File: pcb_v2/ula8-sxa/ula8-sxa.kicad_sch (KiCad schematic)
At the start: 7 parts, among them J1 ula8a, U1 74LS244

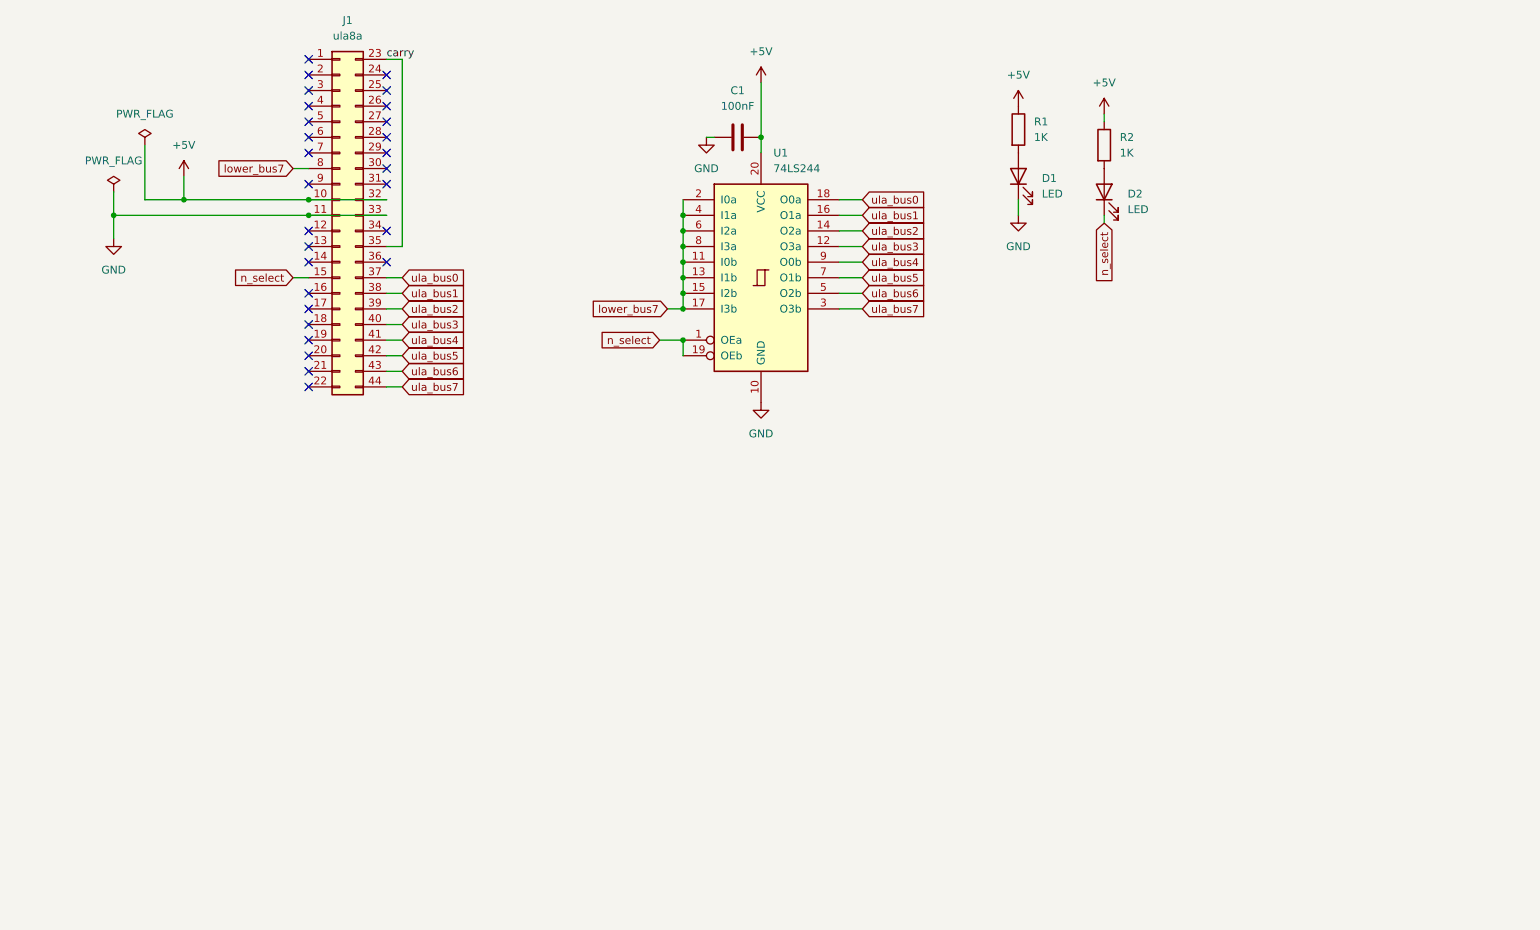
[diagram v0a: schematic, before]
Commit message: deslocando alimentação para as estremidades do conector; carry out em três estados (ativo apenas quando select)
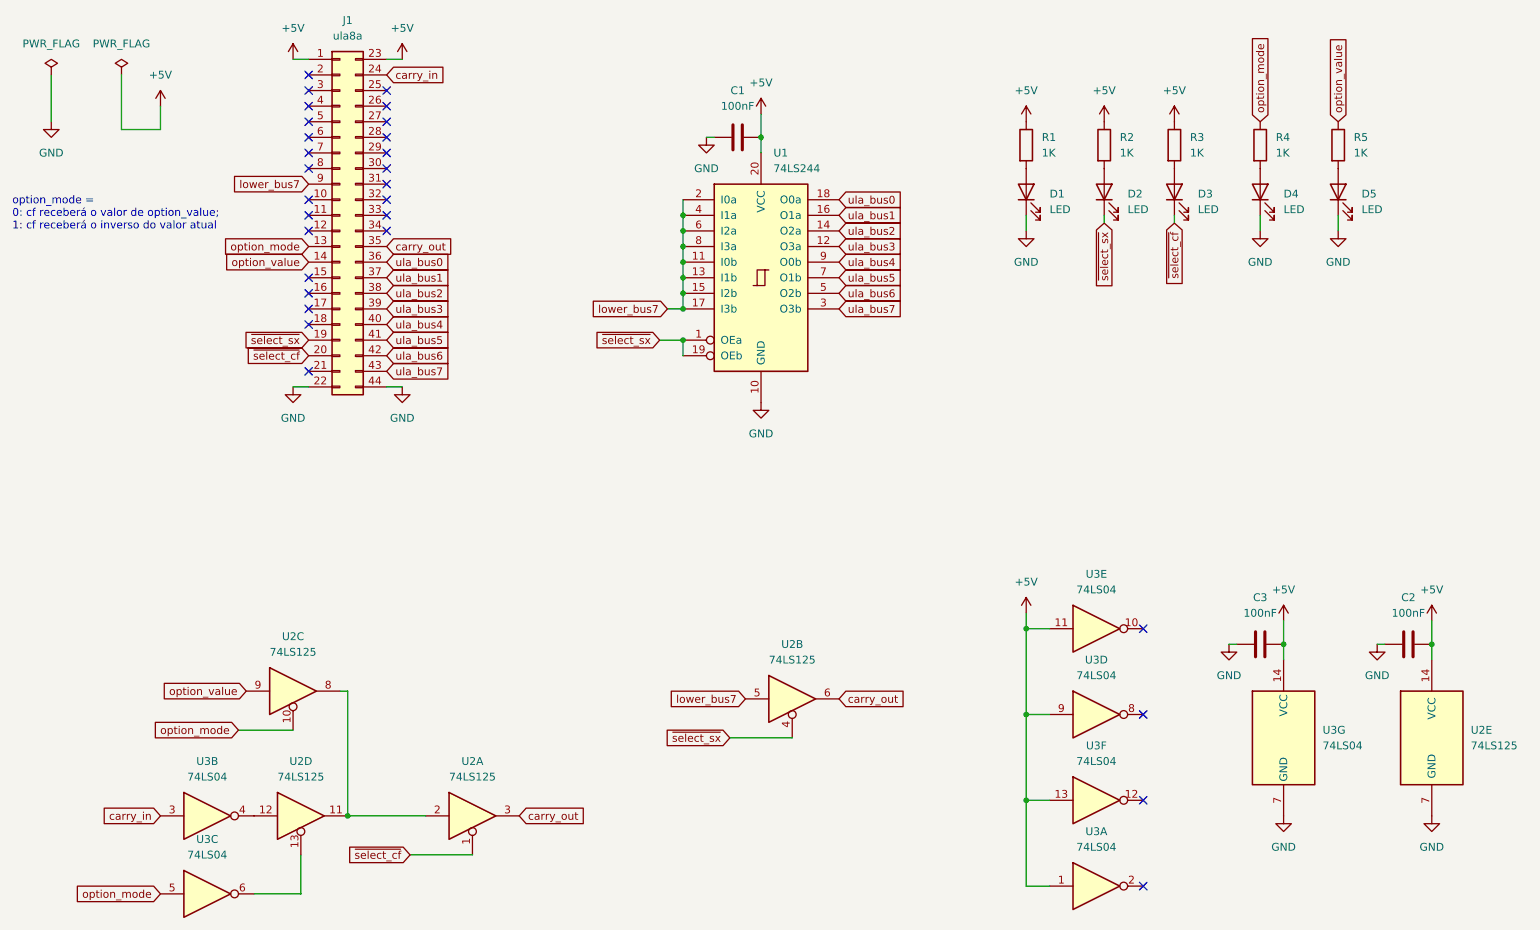
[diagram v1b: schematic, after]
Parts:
- added C2, C3: 100nF, Capacitor_THT:C_Disc_D5.1mm_W3.2mm_P5.00mm, symbol Device:C
- added D3, D4, D5: LED, LED_THT:LED_D5.0mm, symbol Device:LED
- added R3, R4, R5: 1K, Resistor_THT:R_Axial_DIN0207_L6.3mm_D2.5mm_P7.62mm_Horizontal, symbol Device:R
- added U2: 74LS125, Package_DIP:DIP-14_W7.62mm, symbol 74xx:74LS125
- added U3: 74LS04, Package_DIP:DIP-14_W7.62mm, symbol 74xx:74LS04
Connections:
- net +5V: now also J1.1 (Pin_1), J1.23 (Pin_23), C2.2, C3.2, R3.1, U2.14 (VCC), U3.1, U3.11, U3.13, U3.14 (VCC), U3.9; no longer J1.10 (Pin_10), J1.32 (Pin_32)
- net GND: now also J1.22 (Pin_22), J1.44 (Pin_44), C2.1, C3.1, D4.1 (K), D5.1 (K), U2.7 (GND), U3.7 (GND); no longer J1.11 (Pin_11), J1.33 (Pin_33)
- net lower_bus7: now also J1.9 (Pin_9), U2.5; no longer J1.8 (Pin_8)
- net ula_bus0: now also J1.36 (Pin_36); no longer J1.37 (Pin_37)
- net ula_bus1: now also J1.37 (Pin_37); no longer J1.38 (Pin_38)
- net ula_bus2: now also J1.38 (Pin_38); no longer J1.39 (Pin_39)
- net ula_bus3: now also J1.39 (Pin_39); no longer J1.40 (Pin_40)
- net ula_bus4: now also J1.40 (Pin_40); no longer J1.41 (Pin_41)
- net ula_bus5: now also J1.41 (Pin_41); no longer J1.42 (Pin_42)
- net ula_bus6: now also J1.42 (Pin_42); no longer J1.43 (Pin_43)
- net ula_bus7: now also J1.43 (Pin_43); no longer J1.44 (Pin_44)
- net option_mode: now reaches J1.13 (Pin_13)
- net option_mode: now also R4.1, U2.10, U3.5
- net option_value: now reaches J1.14 (Pin_14)
- net option_value: now also R5.1, U2.9
- net ~{select_sx}: now reaches J1.19 (Pin_19)
- net ~{select_sx}: now also D2.1 (K), U1.1 (OEa), U1.19 (OEb), U2.4
- net ~{select_cf}: now reaches J1.20 (Pin_20)
- net ~{select_cf}: now also D3.1 (K), U2.1
- net carry_in: now reaches J1.24 (Pin_24)
- net carry_in: now also U3.3
- net carry renamed carry_out
- net carry_out: now also U2.3, U2.6; no longer J1.23 (Pin_23)
- removed net n_select: D2.1 (K), J1.15 (Pin_15), U1.1 (OEa), U1.19 (OEb)
- new net: D5.2 (A), R5.2
- new net: U2.11, U2.2, U2.8
- new net: D4.2 (A), R4.2
- new net: D3.2 (A), R3.2
- new net: U2.12, U3.4
- new net: U2.13, U3.6
- no-connect marks 28 -> 29
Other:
- note added: "option_mode = 0: cf receberá o valor de option_value; 1: cf receberá o inverso do valor atual"
- moved on the sheet: D1, R1
